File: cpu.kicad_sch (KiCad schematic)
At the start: 39 parts, among them J11 Debug, J12 GPS_Snoop, J13 I2C_Snoop, J14 Boot, J6 USB_C_Receptacle_16P, U4 STM32H503KBUx, Y1 32768Hz

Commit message: Sorting out the part placement....
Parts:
- added R16: 100, Resistor_SMD:R_0402_1005Metric, symbol Device:R
- added R19: 100k, Resistor_SMD:R_0402_1005Metric, symbol Device:R
- D5: renamed from D?; footprint (none) -> LED_SMD:LED_RGB_Everlight_EASV3015RGBA0_Horizontal
- D6: footprint (none) -> Diode_SMD:D_SOD-323; JLCPCB (none) -> C19077435
- J11: footprint (none) -> Parts:PinHeader_1x08_P2.54mm_Vertical
- J12: footprint (none) -> Parts:PinHeader_1x03_P2.54mm_Vertical
- J13: footprint (none) -> Parts:PinHeader_1x04_P2.54mm_Vertical; symbol Connector:Conn_01x03_Pin -> Connector:Conn_01x04_Pin; now in the parts list
- J14: footprint (none) -> Connector_PinHeader_2.54mm:PinHeader_1x02_P2.54mm_Vertical
- SW1: renamed from SW?; footprint (none) -> Connector_PinHeader_2.54mm:PinHeader_1x02_P2.54mm_Vertical
- TP4: renamed from TP?; footprint (none) -> Parts:TestPoint
- gave numbers to parts that had none: 26
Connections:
- net +3V3: now also U4.1 (VDD), U4.17 (VDD), U4.5 (VDDA)
- net GND: now also C6.2, C7.2, C8.2, J13.4 (Pin_4), R19.2; no longer J13.3 (Pin_3)
- net dSWD: now reaches J11.7 (Pin_7), R8.1
- net dRST: now reaches J11.1 (Pin_1), R3.1
- net dRX: now reaches J11.2 (Pin_2), R4.1
- net d3V3: now reaches J11.4 (Pin_4), R6.1
- net EN_OUT3: now reaches U4.11 (PA5)
- net dTX: now reaches J11.3 (Pin_3), R5.1
- net dSWC: now reaches J11.6 (Pin_6), R7.1
- new net: J13.3 (Pin_3), R16.1
- new net PDN: R16.2, R19.1
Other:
- note added: "TODO - part and footprint"
- note added: "TODO - put switch on end board?"
- moved on the sheet: C1, C2, C3, C4, C5, C6, C7, C8, D1, D2, D5, D6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

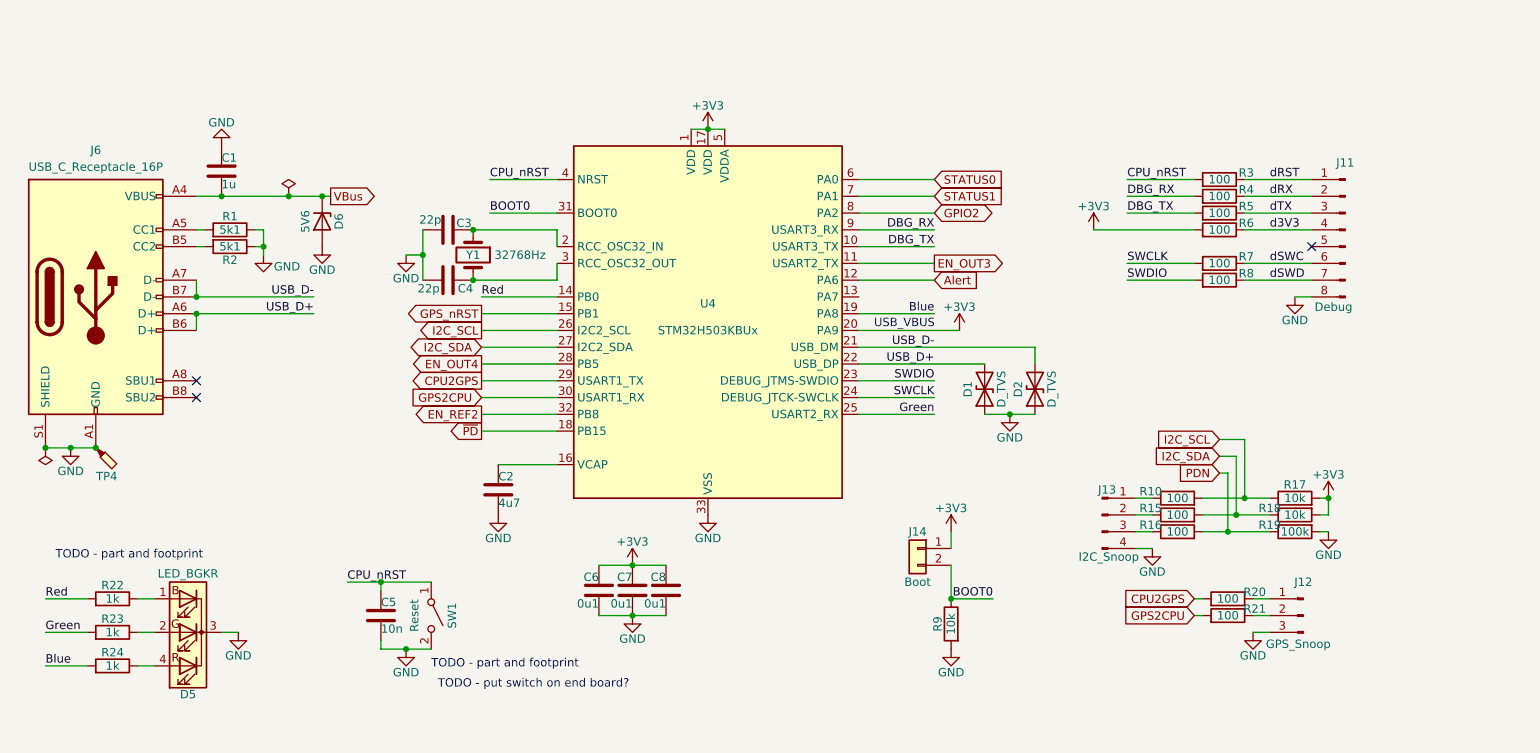
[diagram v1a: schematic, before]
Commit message: First round of component distribution
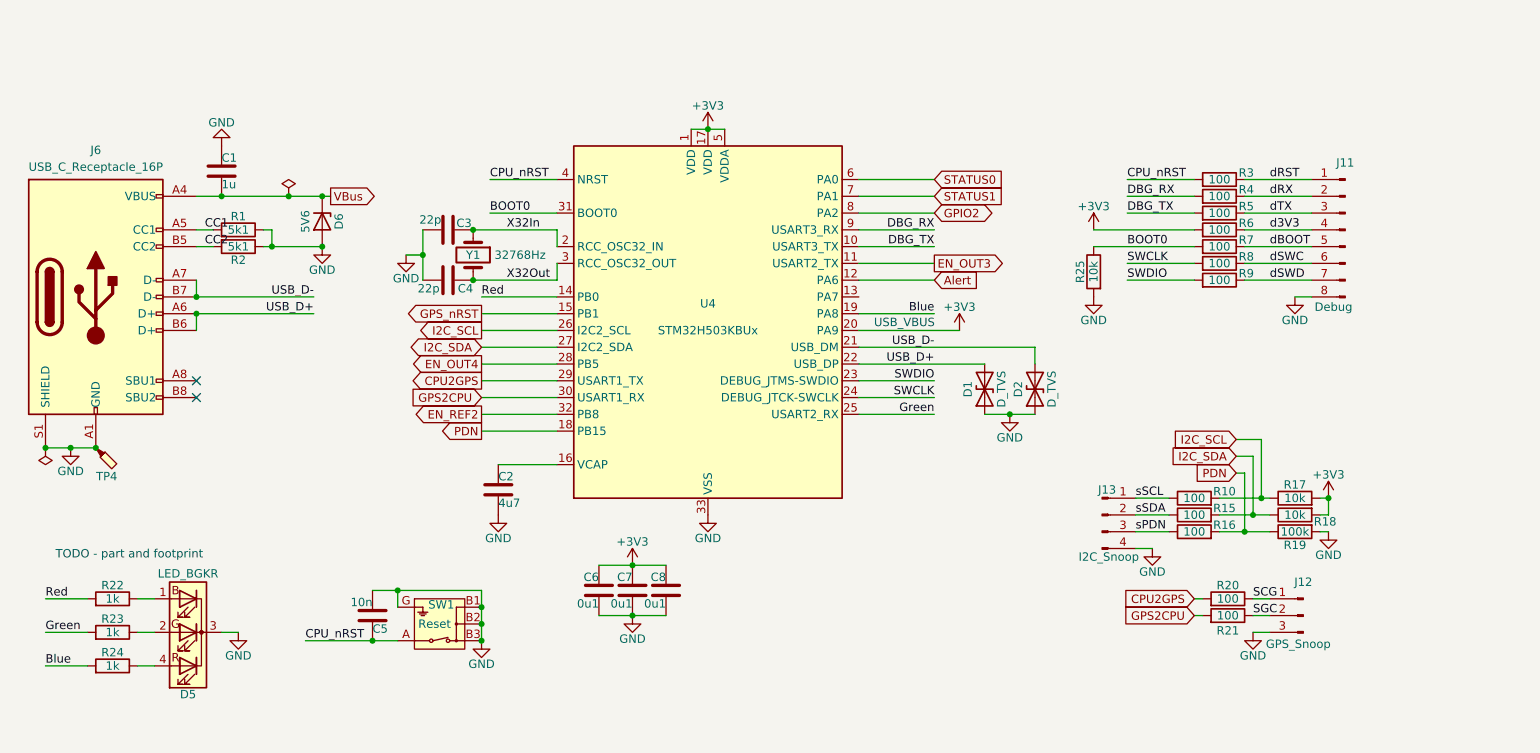
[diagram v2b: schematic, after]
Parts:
- removed J14: Boot, Connector_PinHeader_2.54mm:PinHeader_1x02_P2.54mm_Vertical, symbol Connector_Generic:Conn_01x02
- added R9: 100, Resistor_SMD:R_0402_1005Metric, symbol Device:R
- SW1: footprint Connector_PinHeader_2.54mm:PinHeader_1x02_P2.54mm_Vertical -> Parts:SOU-242HNT_MIT; symbol Switch:SW_SPST -> Parts:SOU-242HNT; now in the parts list
- renumbered R9 to R25
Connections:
- net ~{PD} is gone; now on net PDN: U4.18 (PB15)
- net BOOT0: now also R7.2
- net CPU_nRST: now also SW1.A; no longer SW1.1 (A)
- net GND: now also SW1.B1, SW1.B2, SW1.B3, SW1.G; no longer SW1.2 (B)
- net SWCLK: now also R8.2; no longer R7.2
- net SWDIO: now also R9.2; no longer R8.2
- net dSWC: now also R8.1; no longer R7.1
- net dSWD: now also R9.1; no longer R8.1
- net X32In: now reaches C3.1, U4.2 (PC14), Y1.1
- net X32Out: now reaches C4.1, U4.3 (PC15), Y1.2
- net SGC: now reaches J12.2 (Pin_2), R21.1
- net SCG: now reaches J12.1 (Pin_1), R20.1
- net sPDN: now reaches J13.3 (Pin_3), R16.1
- net sSCL: now reaches J13.1 (Pin_1), R10.1
- net CC2: now reaches J6.B5 (CC2), R2.2
- net dBOOT: now reaches J11.5 (Pin_5)
- net dBOOT: now also R7.1
- net sSDA: now reaches J13.2 (Pin_2), R15.1
- net CC1: now reaches J6.A5 (CC1), R1.2
- no-connect marks 3 -> 2
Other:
- note removed: "TODO - put switch on end board?"
- moved on the sheet: C5, R1, R10, R15, R16, R2, R25, R7, R8

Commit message: Placement looks sane.
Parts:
- D5: value LED_BGKR -> LED_GBAR; footprint LED_SMD:LED_RGB_Everlight_EASV3015RGBA0_Horizontal -> Parts:LED-QPLB615-RGB; symbol Device:LED_BGKR -> Device:LED_GBAR
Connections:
- net +3V3: now also D5.3 (A)
- net Alert: now also U4.9 (PA3); no longer U4.12 (PA6)
- net Blue: now also R22.2, U4.8 (PA2); no longer R24.2, U4.19 (PA8)
- net CPU2GPS: now also U4.14 (PB0); no longer U4.29 (PB6)
- net DBG_RX: now also U4.25 (PA15(JTDI)); no longer U4.9 (PA3)
- net DBG_TX: now also U4.11 (PA5); no longer U4.10 (PA4)
- net EN_OUT3: now also U4.32 (PB8); no longer U4.11 (PA5)
- net EN_OUT4: now also U4.26 (PB3(JTDO); no longer U4.28 (PB5)
- net EN_REF2: now also U4.27 (PB4(NJTRST)); no longer U4.32 (PB8)
- net GND: no longer D5.3 (K)
- net GPIO2: now also U4.18 (PB15); no longer U4.8 (PA2)
- net GPS2CPU: now also U4.15 (PB1); no longer U4.30 (PB7)
- net GPS_nRST: now also U4.19 (PA8); no longer U4.15 (PB1)
- net Green: now also U4.6 (PA0); no longer U4.25 (PA15(JTDI))
- net I2C_SCL: now also U4.29 (PB6); no longer U4.26 (PB3(JTDO)
- net I2C_SDA: now also U4.30 (PB7); no longer U4.27 (PB4(NJTRST))
- net PDN: now also U4.13 (PA7); no longer U4.18 (PB15)
- net Red: now also R24.2, U4.7 (PA1); no longer R22.2, U4.14 (PB0)
- net STATUS0: now also U4.12 (PA6); no longer U4.6 (PA0)
- net STATUS1: now also U4.10 (PA4); no longer U4.7 (PA1)
- net at D5.1 (GK): now also R23.1; no longer R22.1
- net at D5.2 (BK): now also R22.1; no longer R23.1
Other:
- moved on the sheet: C3, C4, D5, Y1

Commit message: Routing well underway
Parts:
- removed R10, R15, R16: 100, Resistor_SMD:R_0402_1005Metric, symbol Device:R
- removed R19: 100k, Resistor_SMD:R_0402_1005Metric, symbol Device:R
- removed SW1: Reset, Parts:SOU-242HNT_MIT, symbol Parts:SOU-242HNT
- D1, D2: footprint Diode_SMD:D_0402_1005Metric_Pad0.77x0.64mm_HandSolder -> Parts:HHS_0402; symbol Device:D_TVS -> Parts:D_TVS; now in the parts list
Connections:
- net GPIO2 is gone; now on net GPS2CPU: U4.18 (PB15)
- net sPDN is gone; now on net PDN: J13.3 (Pin_3)
- net sSCL is gone; now on net I2C_SDA: J13.1 (Pin_1)
- net sSDA is gone; now on net I2C_SCL: J13.2 (Pin_2)
- net Blue: now also U4.6 (PA0); no longer U4.8 (PA2)
- net CPU2GPS: now also U4.19 (PA8); no longer U4.14 (PB0)
- net GND: now also D1.2 (A2), D2.2 (A2); no longer D1.1 (A1), D2.1 (A1)
- net GPS2CPU: no longer U4.15 (PB1)
- net GPS_nRST: now also U4.15 (PB1); no longer U4.19 (PA8)
- net Green: now also U4.7 (PA1); no longer U4.6 (PA0)
- net I2C_SCL: now also R18.1; no longer R17.1
- net I2C_SDA: now also R17.1; no longer R18.1
- net PDN: now also U4.10 (PA4); no longer U4.13 (PA7)
- net Red: now also U4.8 (PA2); no longer U4.7 (PA1)
- net STATUS0: now also U4.14 (PB0); no longer U4.12 (PA6)
- net STATUS1: now also U4.12 (PA6); no longer U4.10 (PA4)
- net USB_D+: now also D1.1 (A1); no longer D1.2 (A2)
- net USB_D-: now also D2.1 (A1); no longer D2.2 (A2)
- no-connect marks 2 -> 3
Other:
- note removed: "TODO - part and footprint"
- moved on the sheet: C5, C6, C7, C8, D5, J11, J12, J13, R17, R18, R20, R21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

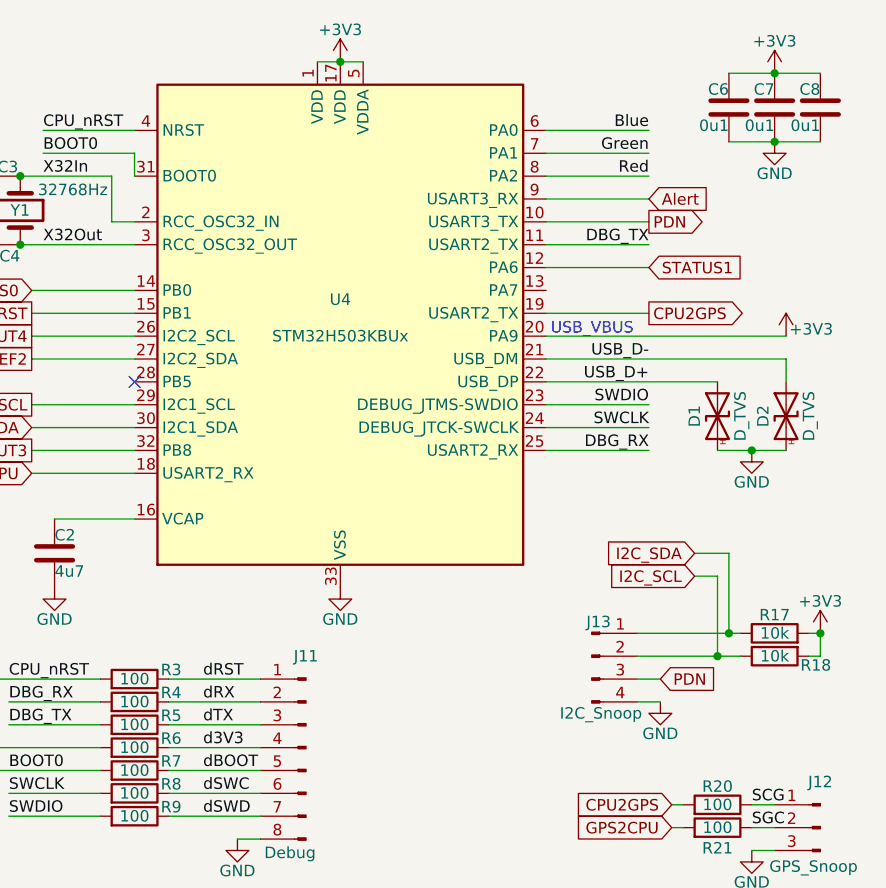
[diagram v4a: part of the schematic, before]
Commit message: Supercap is back
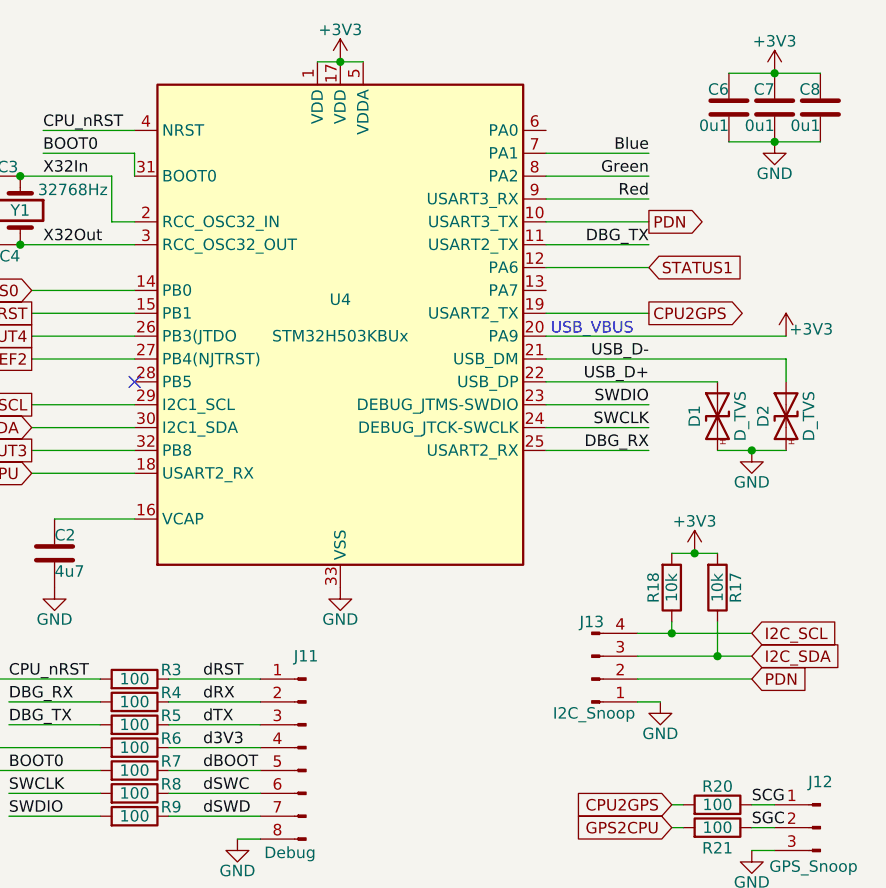
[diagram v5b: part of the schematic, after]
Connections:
- net Alert is gone; now on net Red: U4.9 (PA3)
- net Blue: now also U4.7 (PA1); no longer U4.6 (PA0)
- net GND: now also J13.1 (Pin_1); no longer J13.4 (Pin_4)
- net Green: now also U4.8 (PA2); no longer U4.7 (PA1)
- net I2C_SCL: now also J13.4 (Pin_4); no longer J13.2 (Pin_2)
- net I2C_SDA: now also J13.3 (Pin_3); no longer J13.1 (Pin_1)
- net PDN: now also J13.2 (Pin_2); no longer J13.3 (Pin_3)
- net Red: no longer U4.8 (PA2)
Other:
- moved on the sheet: R17, R18

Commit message: Down to the dregs and clean-ups.
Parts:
- added C9: 1u, Capacitor_SMD:C_0402_1005Metric, symbol Device:C
- C1: JLCPCB (none) -> C52923
- C5: JLCPCB (none) -> C15195
- C6, C7, C8: JLCPCB (none) -> C307331
- D1, D2, D5, J13: now left out of the parts list
- R1, R2: JLCPCB (none) -> C25905
- R17, R18, R25: JLCPCB (none) -> C25744
- R20, R21, R3, R4, R5, R6, R7, R8, R9: JLCPCB (none) -> C25076
- R22, R23, R24: JLCPCB (none) -> C11702
- U4: JLCPCB (none) -> C22385521
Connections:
- net GND: now also C9.1
- net VBus: now also C9.2

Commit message: Add a U.Fl connector for fun.
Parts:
- renumbered J6 to J7
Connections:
- net GND: now also U4.13 (PA7)
- no-connect marks 3 -> 4

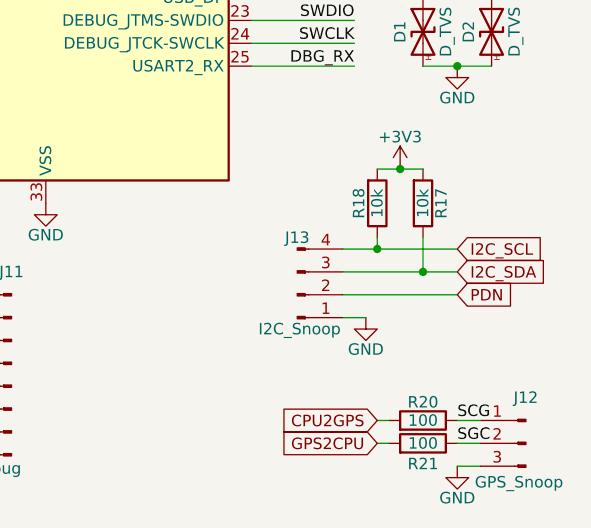
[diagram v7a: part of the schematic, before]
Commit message: DRC clean-up.  Only silk-screen noise left.
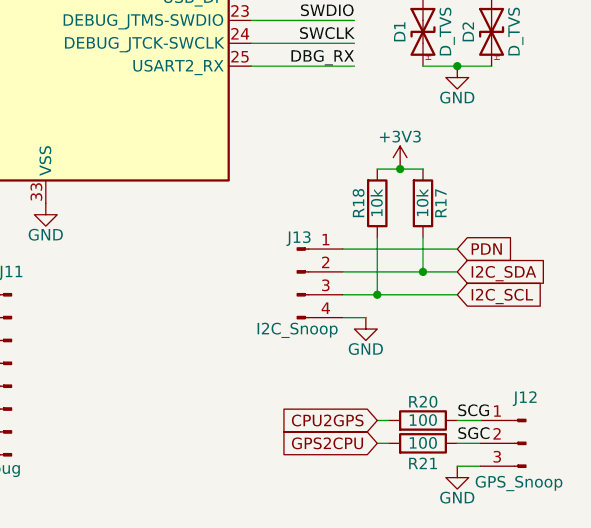
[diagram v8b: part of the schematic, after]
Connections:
- net GND: now also J13.4 (Pin_4); no longer J13.1 (Pin_1)
- net I2C_SCL: now also J13.3 (Pin_3); no longer J13.4 (Pin_4)
- net I2C_SDA: now also J13.2 (Pin_2); no longer J13.3 (Pin_3)
- net PDN: now also J13.1 (Pin_1); no longer J13.2 (Pin_2)
